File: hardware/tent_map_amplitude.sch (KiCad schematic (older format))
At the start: 53 parts, among them U1 LM339AN, U2 TL082IP, U3 TL082IP, U4 LF398_DIP8, U5 LF398_DIP8, U6 LF398_DIP8

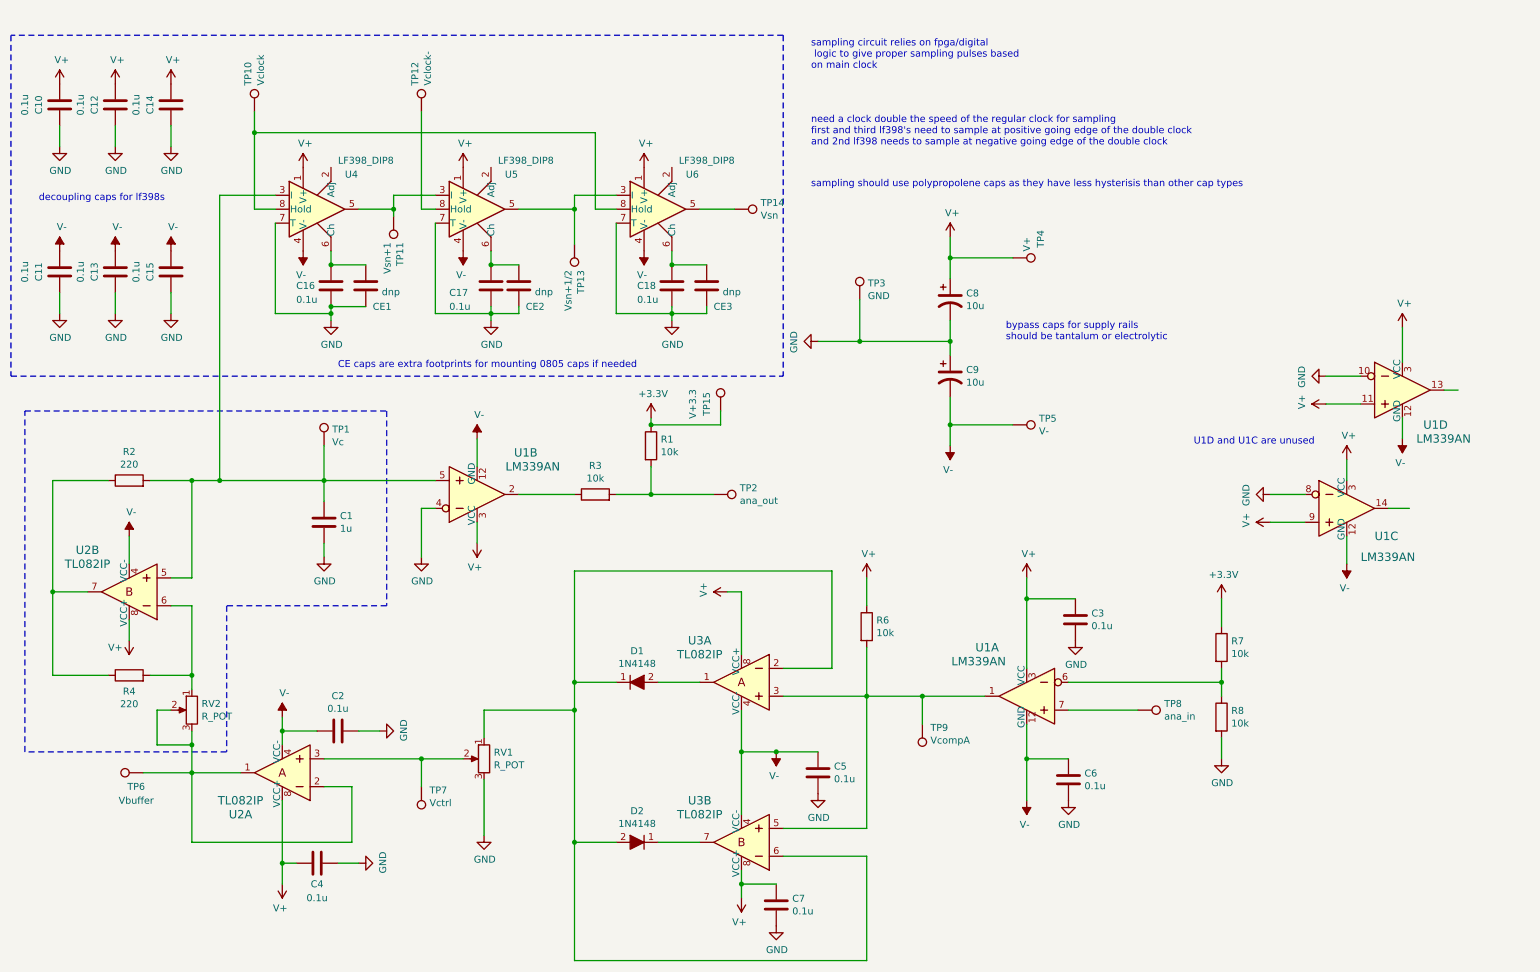
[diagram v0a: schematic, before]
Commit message: Use extra comparator for sampled bitstream output
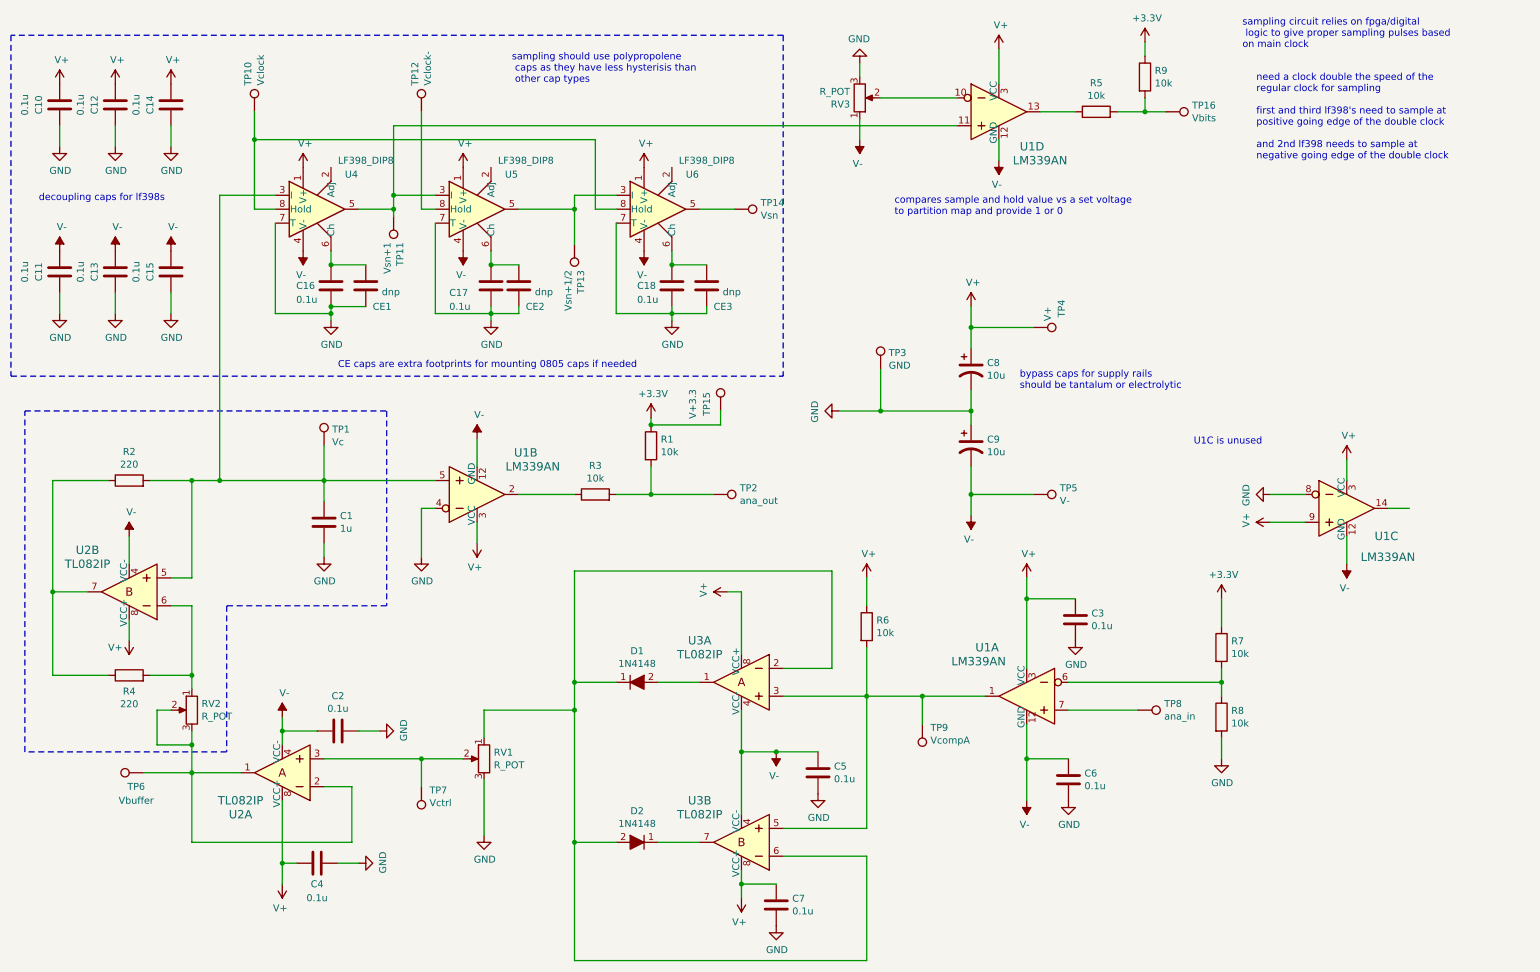
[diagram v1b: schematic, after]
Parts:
- added R5, R9: 10k, Resistor_SMD:R_0805_2012Metric_Pad1.20x1.40mm_HandSolder, symbol Device:R
- added RV3: R_POT, Potentiometer_THT:Potentiometer_Bourns_3296W_Vertical, symbol Device:R_POT
- added TP16: Vbits, TestPoint:TestPoint_Bridge_Pitch2.54mm_Drill1.0mm, symbol Connector:TestPoint
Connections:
- net +3V3: now also R9.1
- net GND: now also RV3.3; no longer U1.10
- net V+: no longer U1.11
- net V-: now also RV3.1
- net at TP11.1, U4.5, U5.3 (I): now also U1.11
- net at U1.13: now also R5.1
- new net: RV3.2, U1.10
- new net: R5.2, R9.2, TP16.1
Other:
- note added: "U1C is unused"
- note added: "compares sample and hold value vs a set voltage \nto partition map and provide 1 or 0"
- note added: "need a clock double the speed of the \nregular clock for sampling\n\nfirst and third lf398's need to sample at \npositive going edge of the double clock\n\nand 2nd lf398 needs to sample at \nnegative going edge of the double clock"
- note added: "sampling should use polypropolene\n caps as they have less hysterisis than\n other cap types\n"
- note removed: "U1D and U1C are unused"
- note removed: "need a clock double the speed of the regular clock for sampling\nfirst and third lf398's need to sample at positive going edge of the double clock\nand 2nd lf398 needs to sample at negative going edge of the double clock"
- note removed: "sampling should use polypropolene caps as they have less hysterisis than other cap types\n"
- moved on the sheet: C8, C9, TP3, TP4, TP5, U1D
